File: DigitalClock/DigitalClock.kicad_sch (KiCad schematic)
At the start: 58 parts

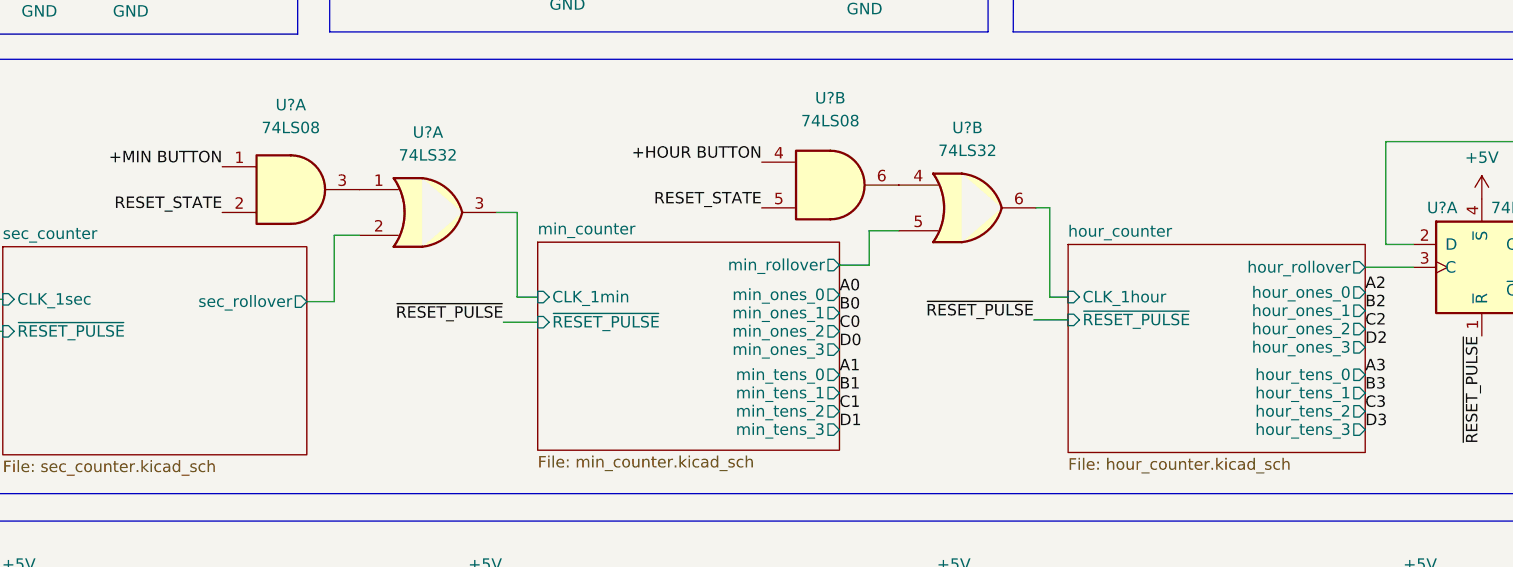
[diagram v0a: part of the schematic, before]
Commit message: added minute counter schematic"
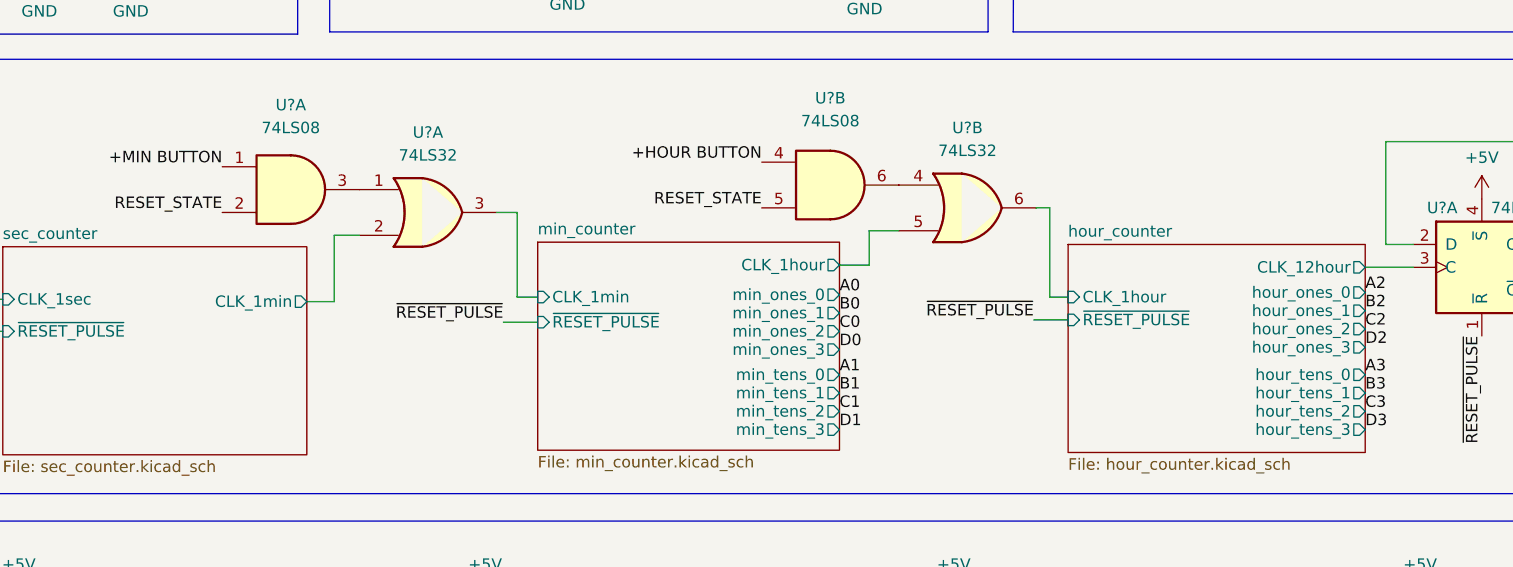
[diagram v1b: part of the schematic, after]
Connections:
- net hour_counter/hour_rollover renamed hour_counter/CLK_12hour
- net min_counter/min_rollover renamed min_counter/CLK_1hour
- net sec_counter/sec_rollover renamed sec_counter/CLK_1min
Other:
- sheet hour_counter ports: added CLK_12hour; removed hour_rollover
- sheet min_counter ports: added CLK_1hour; removed min_rollover
- sheet sec_counter ports: added CLK_1min; removed sec_rollover

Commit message: finished kicad schematic
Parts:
- gave numbers to parts that had none: 46
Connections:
- net +5V: now also U10.7 (DP), U14.7 (DP), U3.7 (DP), U7.7 (DP)
- no-connect marks 0 -> 4

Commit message: about to begin layout
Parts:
- C1, C2, C3, C4: footprint (none) -> Capacitor_THT:C_Disc_D5.0mm_W2.5mm_P5.00mm
- C5, C6, C7: footprint (none) -> Capacitor_THT:CP_Radial_Tantal_D5.0mm_P5.00mm
- D1, D2: footprint (none) -> LED_THT:LED_D3.0mm
- J1: footprint (none) -> TerminalBlock_Phoenix:TerminalBlock_Phoenix_MKDS-1,5-2_1x02_P5.00mm_Horizontal
- R1, R10, R11, R12, R13, R14, R15, R2, R3, R4, R5, R6, R7, R8, R9: footprint (none) -> Resistor_THT:R_Axial_DIN0207_L6.3mm_D2.5mm_P10.16mm_Horizontal
- SW1, SW2, SW3: footprint (none) -> Button_Switch_THT:Push_E-Switch_KS01Q01
- U1, U12, U6, U8: footprint (none) -> Package_DIP:DIP-16_W7.62mm
- U10, U14, U3, U7: footprint Display_7Segment:HDSP-7801 -> Display_7Segment:7SegmentLED_LTS6760_LTS6780
- U11: footprint (none) -> Package_TO_SOT_THT:TO-220-3_Vertical
- U13, U15, U4, U5, U9: footprint (none) -> Package_DIP:DIP-14_W7.62mm

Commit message: more routing
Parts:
- added R16, R17, R18, R19, R20, R21, R22, R23, R24, R25, R26, R27, R28, R29, R30, R31, R32, R33, R34, R35, R36, R37, R38, R39, R40, R41, R42, R43: 1k, Resistor_THT:R_Axial_DIN0207_L6.3mm_D2.5mm_P10.16mm_Horizontal, symbol Device:R_Small_US
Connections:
- net at U7.10 (A): now also R23.2; no longer U6.13 (a)
- net at U7.2 (F): now also R28.2; no longer U6.15 (f)
- net at U7.3 (G): now also R29.2; no longer U6.14 (g)
- net at U7.4 (E): now also R27.2; no longer U6.9 (e)
- net at U7.5 (D): now also R26.2; no longer U6.10 (d)
- net at U7.8 (C): now also R25.2; no longer U6.11 (c)
- net at U7.9 (B): now also R24.2; no longer U6.12 (b)
- net at U1.10 (d): now also R19.1; no longer U3.5 (D)
- net at U1.11 (c): now also R18.1; no longer U3.8 (C)
- net at U1.12 (b): now also R17.1; no longer U3.9 (B)
- net at U1.13 (a): now also R16.1; no longer U3.10 (A)
- net at U1.14 (g): now also R22.1; no longer U3.3 (G)
- net at U1.15 (f): now also R21.1; no longer U3.2 (F)
- net at U1.9 (e): now also R20.1; no longer U3.4 (E)
- net at U8.13 (a): now also R30.1; no longer U10.10 (A)
- net at U10.2 (F): now also R35.2; no longer U8.15 (f)
- net at U8.14 (g): now also R36.1; no longer U10.3 (G)
- net at U10.4 (E): now also R34.2; no longer U8.9 (e)
- net at U8.10 (d): now also R33.1; no longer U10.5 (D)
- net at U10.8 (C): now also R32.2; no longer U8.11 (c)
- net at U10.9 (B): now also R31.2; no longer U8.12 (b)
- net at U14.10 (A): now also R37.2; no longer U12.13 (a)
- net at U14.2 (F): now also R42.2; no longer U12.15 (f)
- net at U12.14 (g): now also R43.1; no longer U14.3 (G)
- net at U12.9 (e): now also R41.1; no longer U14.4 (E)
- net at U14.5 (D): now also R40.2; no longer U12.10 (d)
- net at U14.8 (C): now also R39.2; no longer U12.11 (c)
- net at U12.12 (b): now also R38.1; no longer U14.9 (B)
- new net: R43.2, U14.3 (G)
- new net: R41.2, U14.4 (E)
- new net: R36.2, U10.3 (G)
- new net: R22.2, U3.3 (G)
- new net: R30.2, U10.10 (A)
- new net: R33.2, U10.5 (D)
- new net: R23.1, U6.13 (a)
- new net: R38.2, U14.9 (B)
- new net: R29.1, U6.14 (g)
- new net: R25.1, U6.11 (c)
- new net: R32.1, U8.11 (c)
- new net: R31.1, U8.12 (b)
- new net: R35.1, U8.15 (f)
- new net: R34.1, U8.9 (e)
- new net: R27.1, U6.9 (e)
- new net: R26.1, U6.10 (d)
- new net: R28.1, U6.15 (f)
- new net: R40.1, U12.10 (d)
- new net: R39.1, U12.11 (c)
- new net: R37.1, U12.13 (a)
- new net: R42.1, U12.15 (f)
- new net: R18.2, U3.8 (C)
- new net: R24.1, U6.12 (b)
- new net: R17.2, U3.9 (B)
- new net: R20.2, U3.4 (E)
- new net: R16.2, U3.10 (A)
- new net: R21.2, U3.2 (F)
- new net: R19.2, U3.5 (D)
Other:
- moved on the sheet: U10, U12, U14, U3, U6, U7, U8

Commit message: more layout
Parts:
- removed SW1: +HOUR, Button_Switch_THT:Push_E-Switch_KS01Q01, symbol Switch:SW_DPST
- removed SW2: SET TIME, Button_Switch_THT:Push_E-Switch_KS01Q01, symbol Switch:SW_DPST
- removed SW3: +MIN, Button_Switch_THT:Push_E-Switch_KS01Q01, symbol Switch:SW_DPST
- added SW1, SW2, SW3: SW_Push, Button_Switch_THT:SW_PUSH_6mm, symbol Switch:SW_Push
- added U54: 74LS04, Package_DIP:DIP-14_W7.62mm, symbol 74xx:74LS04
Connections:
- net +5V: now also R1.2, R2.2, R3.2, U54.14 (VCC)
- net +HOUR: now also U54.6; no longer C2.1, R4.2
- net +MIN: now also U54.4; no longer C4.1, R6.2
- net GND: now also SW1.1, SW2.1, SW3.1, U54.11, U54.13, U54.7 (GND), U54.9; no longer R1.2, R2.2, R3.2
- net RESET_BUTTON: now also U54.2; no longer C3.1, R5.2
- net at R3.1, R6.1: now also SW3.2
- net at R2.1, R5.1: now also SW2.2
- new net: C4.1, R6.2, U54.3
- new net: C2.1, R4.2, U54.5
- new net: C3.1, R5.2, U54.1
- no-connect marks 4 -> 7
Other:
- moved on the sheet: C6, C7, D1, D2, J1, Q2, Q3, R1, R11, R13, R14, R15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

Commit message: started routing
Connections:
- net at SW1.2: now also R1.1, R4.1
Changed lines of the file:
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@@
 (kicad_sch (version 20211123) (generator eeschema)
   (paper "A3")
-  (junction (at 38.989 103.886) (diameter 0) (color 0 0 0 0)
-  )
   (junction (at 39.116 84.836) (diameter 0) (color 0 0 0 0)
   )
@@
   (junction (at 49.276 65.024) (diameter 0) (color 0 0 0 0)
   )
+  (junction (at 38.862 103.886) (diameter 0) (color 0 0 0 0)
+  )
   (junction (at 49.022 103.886) (diameter 0) (color 0 0 0 0)
   )
@@
   )
   (junction (at 39.116 65.024) (diameter 0) (color 0 0 0 0)
-  )
-  (junction (at 41.402 103.886) (diameter 0) (color 0 0 0 0)
   )
   (junction (at 94.234 245.618) (diameter 0) (color 0 0 0 0)
@@
     (stroke (width 0) (type default) (color 0 0 0 0))
   )
-  (wire (pts (xy 41.402 103.886) (xy 38.989 103.886))
-    (stroke (width 0) (type default) (color 0 0 0 0))
-  )
   (wire (pts (xy 94.234 245.618) (xy 103.632 245.618))
     (stroke (width 0) (type default) (color 0 0 0 0))
@@
     (stroke (width 0) (type default) (color 0 0 0 0))
   )
-  (wire (pts (xy 35.687 103.886) (xy 38.989 103.886))
+  (wire (pts (xy 35.56 103.886) (xy 38.862 103.886))
     (stroke (width 0) (type default) (color 0 0 0 0))
   )
@@
     (stroke (width 0) (type default) (color 0 0 0 0))
   )
-  (wire (pts (xy 41.529 103.886) (xy 41.402 103.886))
-    (stroke (width 0) (type default) (color 0 0 0 0))
-  )
   (wire (pts (xy 74.676 254.508) (xy 74.676 255.778))
     (stroke (width 0) (type default) (color 0 0 0 0))
@@
     (stroke (width 0) (type default) (color 0 0 0 0))
   )
-  (wire (pts (xy 38.989 102.362) (xy 38.989 103.886))
+  (wire (pts (xy 38.862 102.362) (xy 38.862 103.886))
     (stroke (width 0) (type default) (color 0 0 0 0))
   )
@@
   )
   (polyline (pts (xy 167.513 80.518) (xy 223.647 80.518))
+    (stroke (width 0) (type default) (color 0 0 0 0))
+  )
+  (wire (pts (xy 38.862 103.886) (xy 41.402 103.886))
     (stroke (width 0) (type default) (color 0 0 0 0))
   )
@@
     (pin "2")
   )
-  (symbol (lib_id "Device:R_Small_US") (at 38.989 99.822 0) (mirror x) (unit 1)
-    (in_bom yes) (on_board yes) (fields_autoplaced)
-    (property "Reference" "R1" (id 0) (at 41.021 101.0921 0)
-      (effects (font (size 1.27 1.27)) (justify left))
-    )
-    (property "Value" "10k" (id 1) (at 41.021 98.5521 0)
-      (effects (font (size 1.27 1.27)) (justify left))
-    )
-    (property "Footprint" "Resistor_THT:R_Axial_DIN0207_L6.3mm_D2.5mm_P10.16mm_Horizontal" (id 2) (at 38.989 99.822 0)
-      (effects (font (size 1.27 1.27)) hide)
-    )
-    (property "Datasheet" "~" (id 3) (at 38.989 99.822 0)
+  (symbol (lib_id "Device:R_Small_US") (at 38.862 99.822 0) (mirror x) (unit 1)
+    (in_bom yes) (on_board yes) (fields_autoplaced)
+    (property "Reference" "R1" (id 0) (at 40.894 101.0921 0)
+      (effects (font (size 1.27 1.27)) (justify left))
+    )
+    (property "Value" "10k" (id 1) (at 40.894 98.5521 0)
+      (effects (font (size 1.27 1.27)) (justify left))
+    )
+    (property "Footprint" "Resistor_THT:R_Axial_DIN0207_L6.3mm_D2.5mm_P10.16mm_Horizontal" (id 2) (at 38.862 99.822 0)
+      (effects (font (size 1.27 1.27)) hide)
+    )
+    (property "Datasheet" "~" (id 3) (at 38.862 99.822 0)
       (effects (font (size 1.27 1.27)) hide)
     )
@@
     (pin "3")
   )
-  (symbol (lib_id "power:+5V") (at 38.989 97.282 0) (unit 1)
-    (in_bom yes) (on_board yes)
-    (property "Reference" "#PWR04" (id 0) (at 38.989 101.092 0)
-      (effects (font (size 1.27 1.27)) hide)
-    )
-    (property "Value" "+5V" (id 1) (at 36.322 94.488 0))
-    (property "Footprint" "" (id 2) (at 38.989 97.282 0)
-      (effects (font (size 1.27 1.27)) hide)
-    )
-    (property "Datasheet" "" (id 3) (at 38.989 97.282 0)
-      (effects (font (size 1.27 1.27)) hide)
-    )
+  (symbol (lib_id "power:+5V") (at 38.862 97.282 0) (unit 1)
+    (in_bom yes) (on_board yes)
+    (property "Reference" "#PWR04" (id 0) (at 38.862 101.092 0)
+      (effects (font (size 1.27 1.27)) hide)
+    )
+    (property "Value" "+5V" (id 1) (at 36.195 94.488 0))
+    (property "Footprint" "" (id 2) (at 38.862 97.282 0)
+      (effects (font (size 1.27 1.27)) hide)
+    )
+    (property "Datasheet" "" (id 3) (at 38.862 97.282 0)
+      (effects (font (size 1.27 1.27)) hide)
+    )

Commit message: started routing
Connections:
- net +HOUR BUTTON is gone; now on net +HOUR: U4.4
- net +MIN BUTTON is gone; now on net +MIN: U4.1
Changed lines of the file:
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@@
     (effects (font (size 1.27 1.27)) (justify left bottom))
   )
-  (label "+HOUR BUTTON" (at 119.126 132.588 180)
+  (label "+HOUR" (at 119.126 132.588 180)
     (effects (font (size 1.27 1.27)) (justify right bottom))
   )
@@
     (effects (font (size 1.27 1.27)) (justify left bottom))
   )
-  (label "+MIN BUTTON" (at 59.182 133.096 180)
+  (label "+MIN" (at 59.182 133.096 180)
     (effects (font (size 1.27 1.27)) (justify right bottom))
   )
